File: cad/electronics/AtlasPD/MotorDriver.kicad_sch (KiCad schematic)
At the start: 5 parts, among them J301 Conn_01x06, J302 Conn_01x06, U301 74LS08, U302 DRV8837C, U303 DRV8837C

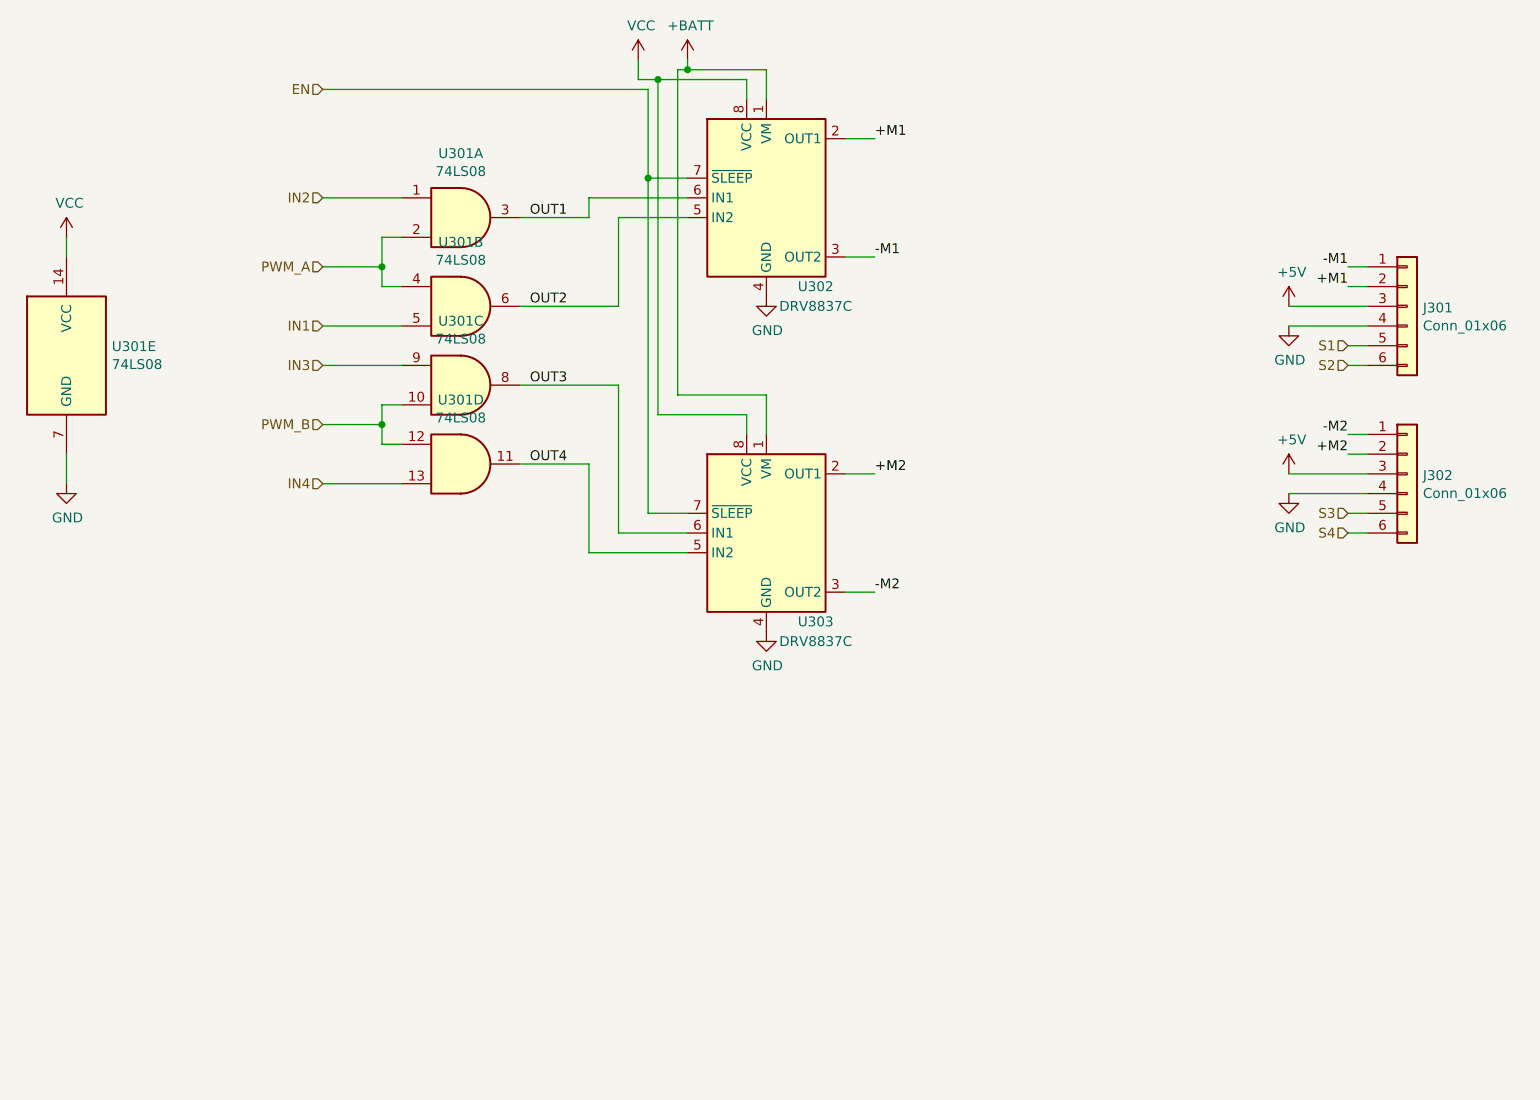
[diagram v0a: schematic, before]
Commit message: Fixed schematic issues from KiCAD upgrade, Moved 3.3V LDO to MCU Sheet
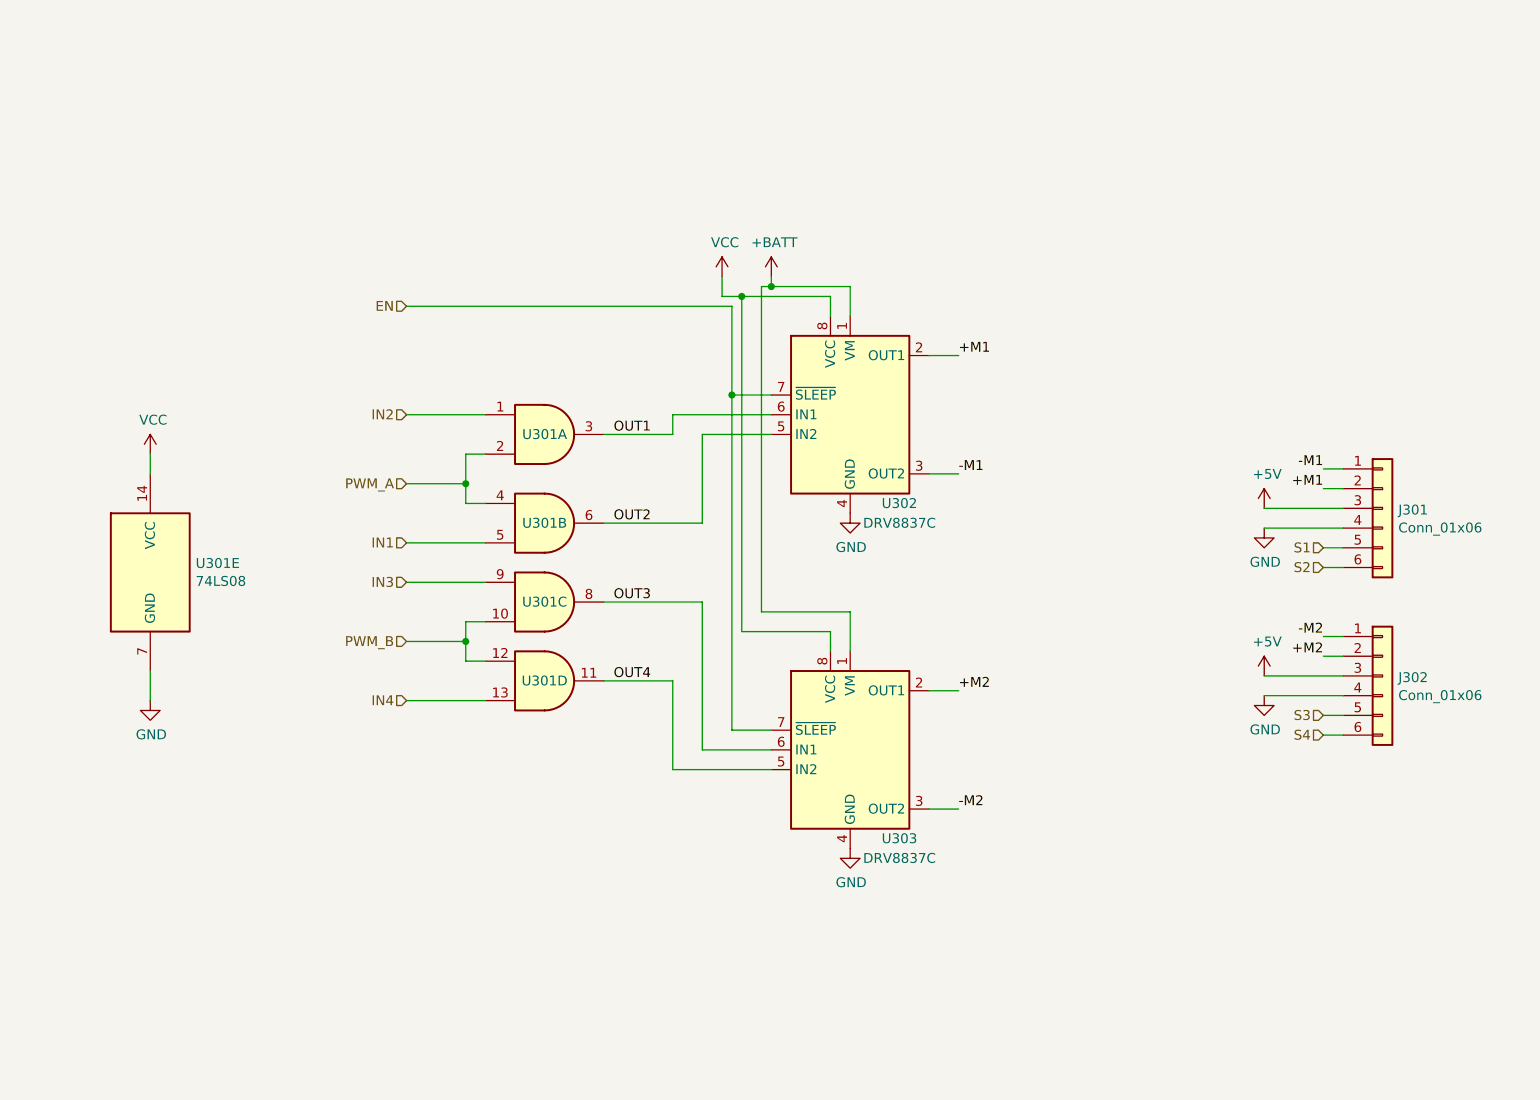
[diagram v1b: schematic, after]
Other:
- moved on the sheet: J301, J302, U301A, U301B, U301C, U301D, U301E, U302, U303

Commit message: Eliminated need for AND gate IC
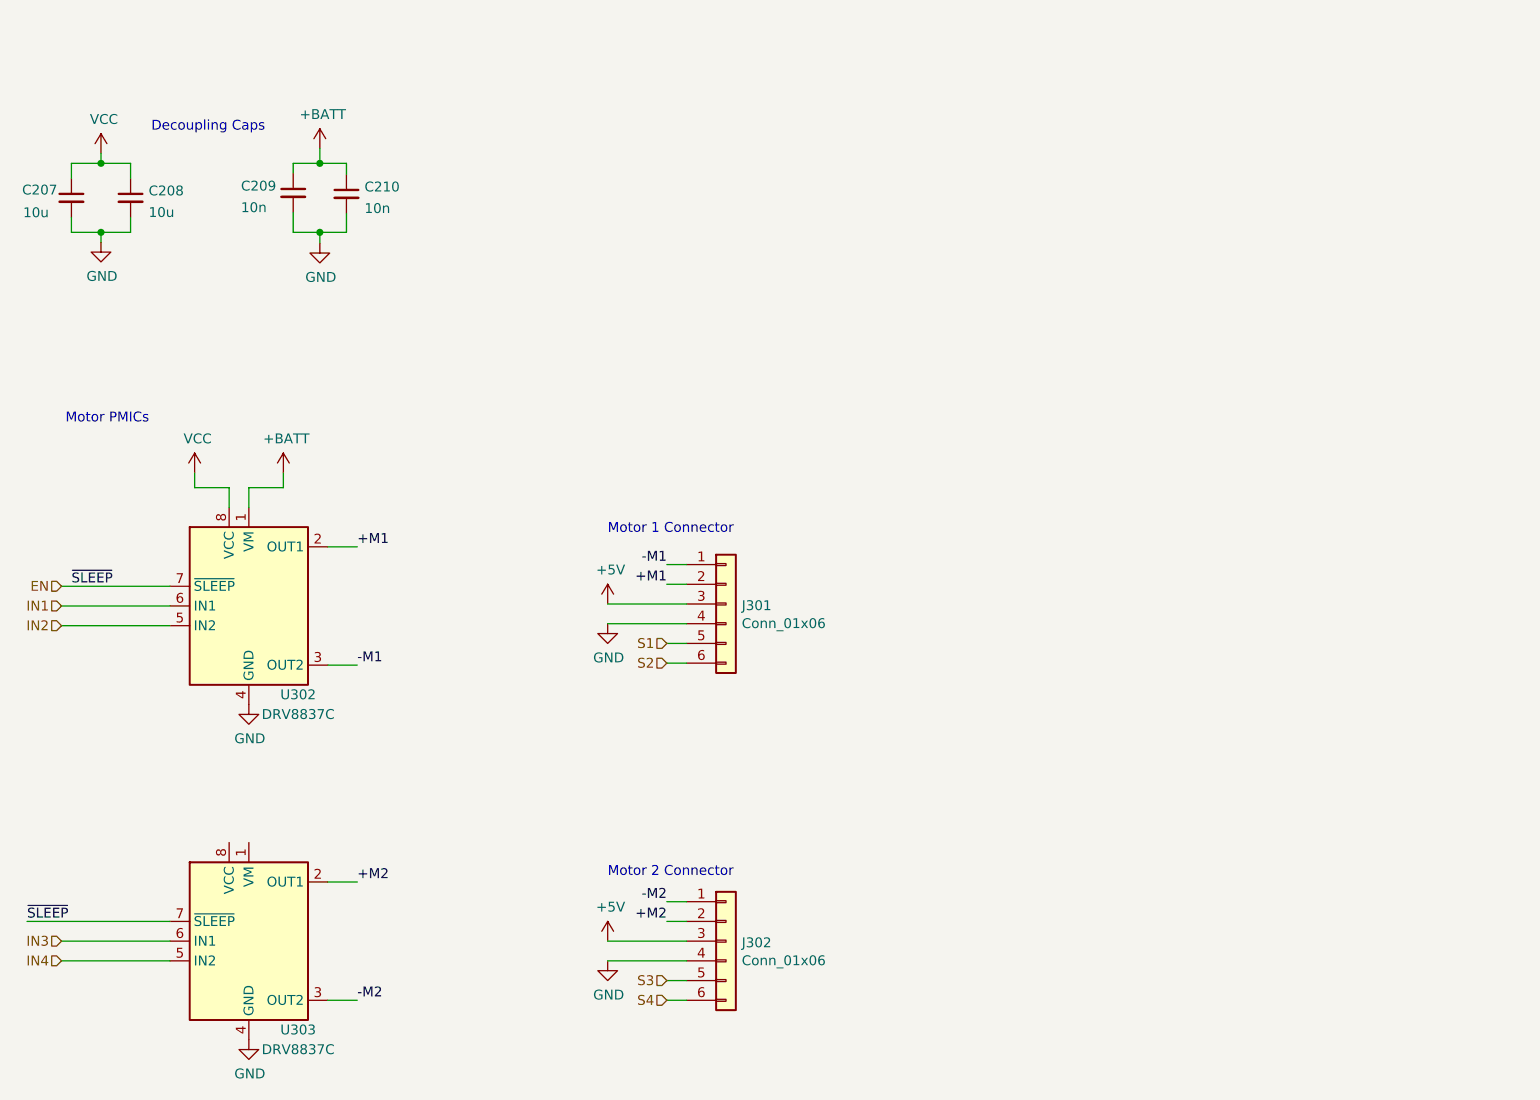
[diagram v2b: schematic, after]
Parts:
- removed U301: 74LS08, Package_SO:SOIC-14_3.9x8.7mm_P1.27mm, symbol 74xx:74LS08
- added C207, C208: 10u, symbol Device:C_Small
- added C209, C210: 10n, symbol Device:C_Small
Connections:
- net OUT1 is gone; now on net IN1: U302.6 (IN1)
- net OUT2 is gone; now on net IN2: U302.5 (IN2)
- net OUT3 is gone; now on net IN3: U303.6 (IN1)
- net OUT4 is gone; now on net IN4: U303.5 (IN2)
- net +BATT: now also C209.1, C210.1; no longer U303.1 (VM)
- net GND: now also C207.2, C208.2, C209.2, C210.2
- net VCC: now also C207.1, C208.1; no longer U303.8 (VCC)
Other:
- note added: "Decoupling Caps"
- note added: "Motor 1 Connector"
- note added: "Motor 2 Connector"
- note added: "Motor PMICs"
- moved on the sheet: J301, J302, U302, U303

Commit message: Small changes
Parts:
- C207, C208, C209, C210: footprint (none) -> Capacitor_SMD:C_0402_1005Metric
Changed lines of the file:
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@@
       (effects (font (size 1.27 1.27)) (justify left))
     )
-    (property "Footprint" "" (id 2) (at 57.15 34.925 0)
+    (property "Footprint" "Capacitor_SMD:C_0402_1005Metric" (id 2) (at 57.15 34.925 0)
       (effects (font (size 1.27 1.27)) hide)
     )
@@
       (effects (font (size 1.27 1.27)) (justify left))
     )
-    (property "Footprint" "" (id 2) (at 36.195 35.56 0)
+    (property "Footprint" "Capacitor_SMD:C_0402_1005Metric" (id 2) (at 36.195 35.56 0)
       (effects (font (size 1.27 1.27)) hide)
     )
@@
       (effects (font (size 1.27 1.27)) (justify left))
     )
-    (property "Footprint" "" (id 2) (at 64.008 35.052 0)
+    (property "Footprint" "Capacitor_SMD:C_0402_1005Metric" (id 2) (at 64.008 35.052 0)
       (effects (font (size 1.27 1.27)) hide)
     )
@@
       (effects (font (size 1.27 1.27)) (justify left))
     )
-    (property "Footprint" "" (id 2) (at 28.575 35.56 0)
+    (property "Footprint" "Capacitor_SMD:C_0402_1005Metric" (id 2) (at 28.575 35.56 0)
       (effects (font (size 1.27 1.27)) hide)
     )
